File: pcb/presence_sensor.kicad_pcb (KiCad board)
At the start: 2 copper layers, 77.5 x 46 mm, 53 parts, among them J1 SEN0395, J2 USB4105, J3 SM04B-SRSS-TB(LF)(SN), J4 USB4105, Q1 MBT3904DW1, SW1 SW_Push, SW2 SW_Push, U1 ESP32-S2-MINI-1, U2 USBLC6-2P6, U3 AMS1117-3.3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

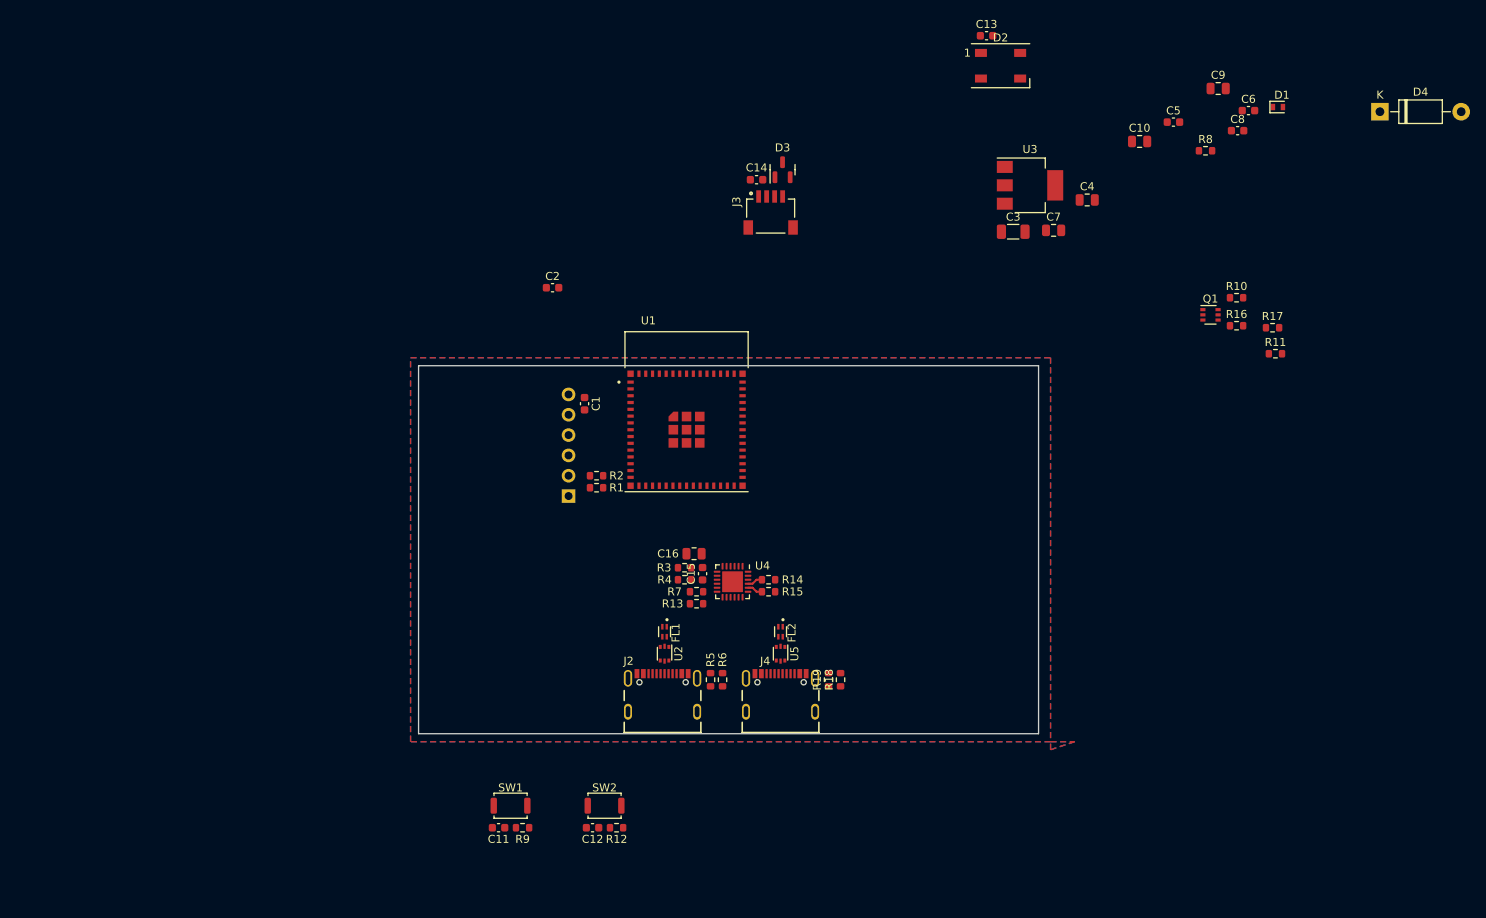
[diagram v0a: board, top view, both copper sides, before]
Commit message: Removed USB TTL
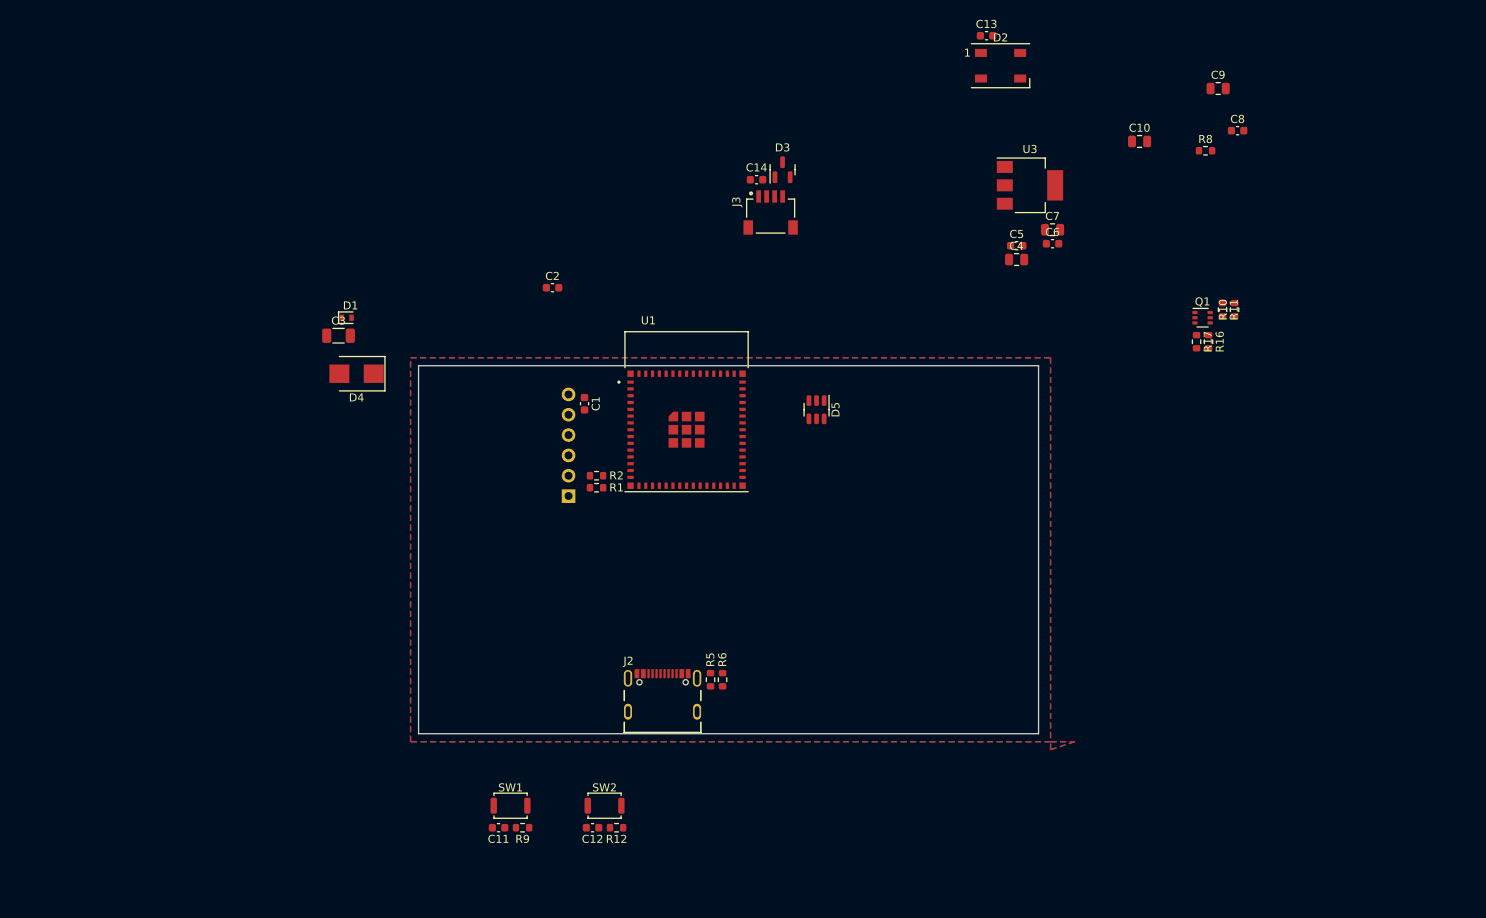
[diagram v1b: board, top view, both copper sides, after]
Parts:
- removed C15: 1u, Capacitor_SMD:C_0603_1608Metric
- removed C16: 10u, Capacitor_SMD:C_0805_2012Metric
- removed FL1, FL2: DLP11SN900HL2L, Presence Sensor:FIL_DLP11SN900HL2L
- removed J4: USB4105, Presence Sensor:GCT_USB4105_REVA
- removed R13, R7: 10K, Resistor_SMD:R_0603_1608Metric
- removed R14, R15: 0R, Resistor_SMD:R_0603_1608Metric
- removed R18, R19: 5.1K, Resistor_SMD:R_0603_1608Metric
- removed R3: 22.1K, Resistor_SMD:R_0603_1608Metric
- removed R4: 47.5K, Resistor_SMD:R_0603_1608Metric
- removed U2, U5: USBLC6-2P6, Package_TO_SOT_SMD:SOT-666
- removed U4: CP2102N-Axx-xQFN24, Package_DFN_QFN:QFN-24-1EP_4x4mm_P0.5mm_EP2.6x2.6mm
- added D5: ESDA6V1-5SC6, Package_TO_SOT_SMD:SOT-23-6, F.Cu at (149.8, 85.5)
- D4: value 1N5819 -> B220; footprint Diode_THT:D_DO-41_SOD81_P10.16mm_Horizontal -> Diode_SMD:D_SMB
- moved D4 132.0 mm to (92.2, 81.0), turned to 180 degrees
- moved D1 119.4 mm to (91.0, 74.0)
- moved C3 85.3 mm to (90.0, 76.2)
- moved C6 29.6 mm to (179.2, 64.8)
- moved C5 24.9 mm to (174.8, 65.0)
- moved C4 11.6 mm to (174.8, 66.7)
- moved R17 9.66 mm to (197.2, 77.0), turned to -90 degrees
- moved R11 8.60 mm to (200.5, 73.0), turned to -90 degrees
- moved R16 4.03 mm to (198.8, 77.0), turned to -90 degrees
- moved R10 1.52 mm to (202.0, 73.0), turned to 90 degrees
- moved Q1 1.05 mm to (198.0, 74.0)
- moved C7 0.15 mm to (179.2, 63.0)
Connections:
- net /~{ESP_DTR} renamed /DTR
- J2 pad A6: /USB_CON_P -> unconnected-(J2-D+)_1
- J2 pad A7: /USB_CON_N -> unconnected-(J2-D-)_1
- J2 pad B6: /USB_CON_P -> unconnected-(J2-D+)
- J2 pad B7: /USB_CON_N -> unconnected-(J2-D-)
- U1 pad 23: /USB_DEV_N -> unconnected-(U1-IO19)
- U1 pad 24: /USB_DEV_P -> unconnected-(U1-IO20)
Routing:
- net Net-(U4-TXD): track 1.94 -> 0.00 mm
- net Net-(U4-RXD): track 1.94 -> 0.00 mm

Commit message: Update
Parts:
- removed D4: B220, Diode_SMD:D_SMB
- added C15: 100n, Capacitor_SMD:C_0603_1608Metric, F.Cu at (53.2, 118.8)
- added C16: 100n, Capacitor_SMD:C_0603_1608Metric, F.Cu at (51.8, 118.8)
- added C17: 12pF, Capacitor_SMD:C_0603_1608Metric, F.Cu at (91.5, 107.0)
- added C18: 12pF, Capacitor_SMD:C_0603_1608Metric, F.Cu at (94.5, 107.0)
- added C19: 100n, Capacitor_SMD:C_0603_1608Metric, F.Cu at (93.8, 130.5)
- added C20: 4.7u, Capacitor_SMD:C_0805_2012Metric, F.Cu at (89.4, 135.8)
- added C21: 100n, Capacitor_SMD:C_0603_1608Metric, F.Cu at (173.2, 120.5)
- added C22: 10u, Capacitor_SMD:C_0805_2012Metric, F.Cu at (154.2, 133.0)
- added C23: 1u, Capacitor_SMD:C_0603_1608Metric, F.Cu at (157.5, 133.8)
- added C24: 100n, Capacitor_SMD:C_0603_1608Metric, F.Cu at (154.8, 130.5)
- added FID1: Fiducial, Fiducial:Fiducial_0.5mm_Mask1mm, B.Cu at (88.2, 145.0)
- added FID2: Fiducial, Fiducial:Fiducial_0.5mm_Mask1mm, F.Cu at (88.2, 145.0)
- added FID3: Fiducial, Fiducial:Fiducial_0.5mm_Mask1mm, B.Cu at (108.0, 83.0)
- added FID4: Fiducial, Fiducial:Fiducial_0.5mm_Mask1mm, F.Cu at (84.0, 83.0)
- added FID5: Fiducial, Fiducial:Fiducial_0.5mm_Mask1mm, B.Cu at (84.0, 83.0)
- added FID6: Fiducial, Fiducial:Fiducial_0.5mm_Mask1mm, F.Cu at (108.0, 83.0)
- added FL1: DLP11SN900HL2L, Presence Sensor:FIL_DLP11SN900HL2L, F.Cu at (96.0, 133.0)
- added H1: MountingHole, MountingHole:MountingHole_2.7mm_M2.5, F.Cu at (85.0, 143.0)
- added H2: MountingHole, MountingHole:MountingHole_2.7mm_M2.5, F.Cu at (107.0, 143.0)
- added H3: MountingHole, MountingHole:MountingHole_2.2mm_M2, F.Cu at (84.0, 118.0)
- added H4: MountingHole, MountingHole:MountingHole_2.2mm_M2, F.Cu at (84.0, 98.0)
- added J4: Conn_01x05, Connector_PinHeader_2.54mm:PinHeader_1x05_P2.54mm_Vertical, F.Cu at (108.2, 90.4)
- added R13: DNP, Resistor_SMD:R_0603_1608Metric, F.Cu at (56.2, 118.8)
- added R14: 10K, Resistor_SMD:R_0603_1608Metric, F.Cu at (177.3, 120.5)
- added R15: 22.1K, Resistor_SMD:R_0603_1608Metric, F.Cu at (156.0, 133.8)
- added R18: 47.5K, Resistor_SMD:R_0603_1608Metric, F.Cu at (159.0, 133.8)
- added R19: 10K, Resistor_SMD:R_0603_1608Metric, F.Cu at (160.2, 133.8)
- added R20: 10K, Resistor_SMD:R_0603_1608Metric, F.Cu at (161.8, 133.8)
- added R21: 0R, Resistor_SMD:R_0603_1608Metric, F.Cu at (159.0, 124.0)
- added R22: 0R, Resistor_SMD:R_0603_1608Metric, F.Cu at (160.5, 124.0)
- added R3: 10K, Resistor_SMD:R_0603_1608Metric, F.Cu at (70.5, 143.0)
- added R4: 4.7K, Resistor_SMD:R_0603_1608Metric, F.Cu at (101.5, 109.5)
- added R7: 4.7K, Resistor_SMD:R_0603_1608Metric, F.Cu at (100.0, 109.5)
- added SW3: SW_SPDT, Button_Switch_SMD:SW_Push_1P1T-SH_NO_CK_KMR2xxG, F.Cu at (168.3, 116.0)
- added U2: USBLC6-2P6, Package_TO_SOT_SMD:SOT-666, F.Cu at (96.0, 136.0)
- added U4: AP2161W, Package_TO_SOT_SMD:SOT-23-5, F.Cu at (70.5, 140.0)
- added U5: BMP280, Package_LGA:Bosch_LGA-8_2x2.5mm_P0.65mm_ClockwisePinNumbering, F.Cu at (52.8, 115.8)
- added U6: FSUSB42UMX, Presence Sensor:IC_FSUSB42UMX, F.Cu at (96.0, 130.5)
- added U7: CP2102N-Axx-xQFN24, Package_DFN_QFN:QFN-24-1EP_4x4mm_P0.5mm_EP2.6x2.6mm, F.Cu at (159.0, 129.2)
- added Y1: 32.768MHz, Presence Sensor:NX3215SA, F.Cu at (93.0, 104.2)
- C3: footprint Capacitor_SMD:C_1206_3216Metric -> Capacitor_SMD:C_0805_2012Metric
- C8: value 100n -> 1u
- moved C8 166.7 mm to (50.2, 118.8), turned to -90 degrees
- moved R8 157.9 mm to (54.8, 118.8), turned to 90 degrees
- moved C9 122.6 mm to (85.0, 88.0), turned to 90 degrees
- moved C10 109.2 mm to (87.0, 88.0), turned to 90 degrees
- moved C4 91.8 mm to (122.5, 142.2)
- moved C5 91.8 mm to (122.5, 140.5)
- moved C6 91.8 mm to (127.0, 140.2)
- moved C7 91.8 mm to (127.0, 138.5)
- moved U3 91.8 mm to (124.2, 132.9)
- moved C13 89.0 mm to (119.0, 111.0)
- moved D2 89.0 mm to (120.8, 114.8)
- moved D3 67.0 mm to (101.8, 106.3), turned to 0 degrees
- moved C14 65.8 mm to (103.0, 109.5), turned to -90 degrees
- moved D1 62.8 mm to (93.6, 136.8), turned to 180 degrees
- moved J3 62.6 mm to (105.0, 107.8), turned to 90 degrees
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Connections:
- C8 pad 1: /EN -> +3V3
- D5 pad 4: /ESP_RXD -> /ESP_TXD
- D5 pad 5: /ESP_TXD -> /ESP_RXD
- J2 pad A6: unconnected-(J2-D+)_1 -> /USB_CON_P
- J2 pad A7: unconnected-(J2-D-)_1 -> /USB_CON_N
- J2 pad B6: unconnected-(J2-D+) -> /USB_CON_P
- J2 pad B7: unconnected-(J2-D-) -> /USB_CON_N
- R8 pad 2: /EN -> Net-(U5-SDO)
- U1 pad 19: unconnected-(U1-IO15) -> /OSC_SLOW_P
- U1 pad 20: unconnected-(U1-IO16) -> /OSC_SLOW_N
- U1 pad 23: unconnected-(U1-IO19) -> /USB_ESP_N
- U1 pad 24: unconnected-(U1-IO20) -> /USB_ESP_P
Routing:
- net /USB_CON_N: track 0.00 -> 7.85 mm
- net Net-(J2-CC1): track 0.00 -> 6.89 mm
- net Net-(J2-CC2): track 0.00 -> 6.89 mm
- net /OSC_SLOW_P: track 0.00 -> 6.58 mm
- net /OSC_SLOW_N: track 0.00 -> 6.56 mm
- net +3V3: track 0.00 -> 6.05 mm, vias 0 -> 2
- net /USB_CON_P: track 0.00 -> 5.13 mm
- net Net-(J1-Pin_2): track 0.00 -> 4.21 mm
- net /SENS_TXD: track 0.00 -> 3.49 mm
- net GND: track 0.00 -> 3.44 mm, vias 0 -> 29
- net /USB_ESP_P: track 0.00 -> 2.17 mm, vias 0 -> 1
- net /USB_ESP_N: track 0.00 -> 2.17 mm, vias 0 -> 1
- net Net-(J1-Pin_1): track 0.00 -> 2.17 mm
- net /SENS_RXD: track 0.00 -> 1.57 mm
- net /USB_HOST_P: track 0.00 -> 1.39 mm
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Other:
- board size 77.5 x 46 mm -> 28 x 65 mm
- board text added: "1"
